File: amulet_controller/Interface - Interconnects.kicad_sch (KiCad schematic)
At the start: 57 parts, among them J10 JST S2B-PH-SM4-TB, J11 Nano-Fit 1x03, J12 Nano-Fit 1x03, J13 SM05B-GHS-TB, J14 PTH 01x02 2.54mm, J6 SM08B-GHS-TB, J7 SM07B-GHS-TB, J8 JST S2B-PH-SM4-TB, J9 SM06B-GHS-TB, SW1 CAS-220TA

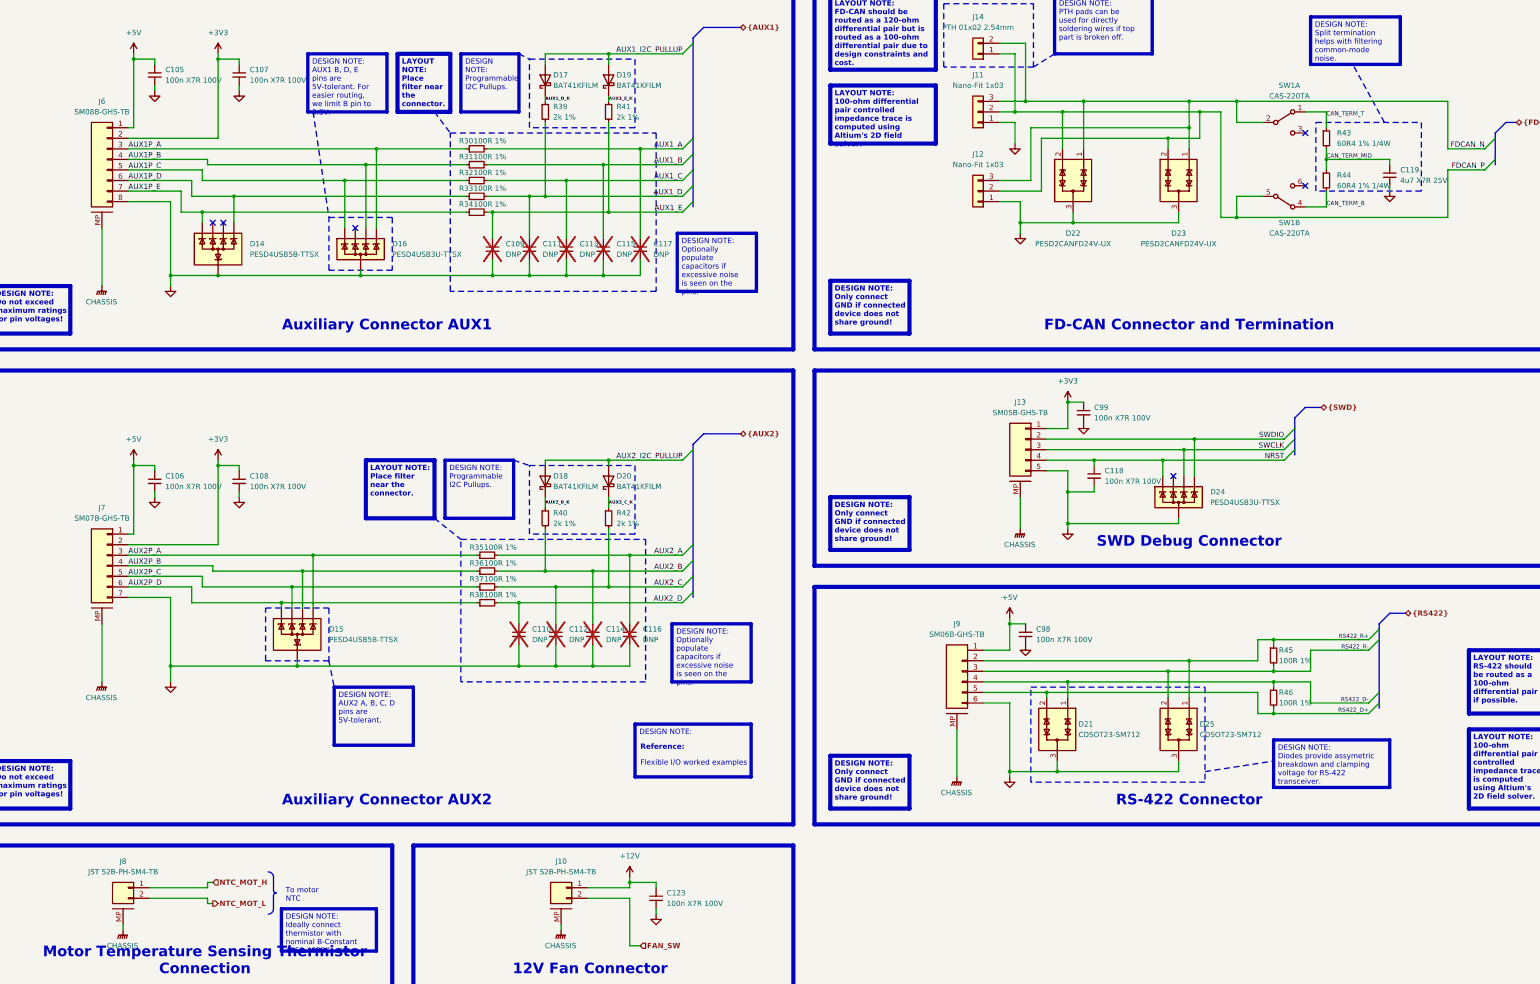
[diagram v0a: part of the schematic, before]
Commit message: filled in fields for bom, replaced inexisting components. Need to replace LEDs
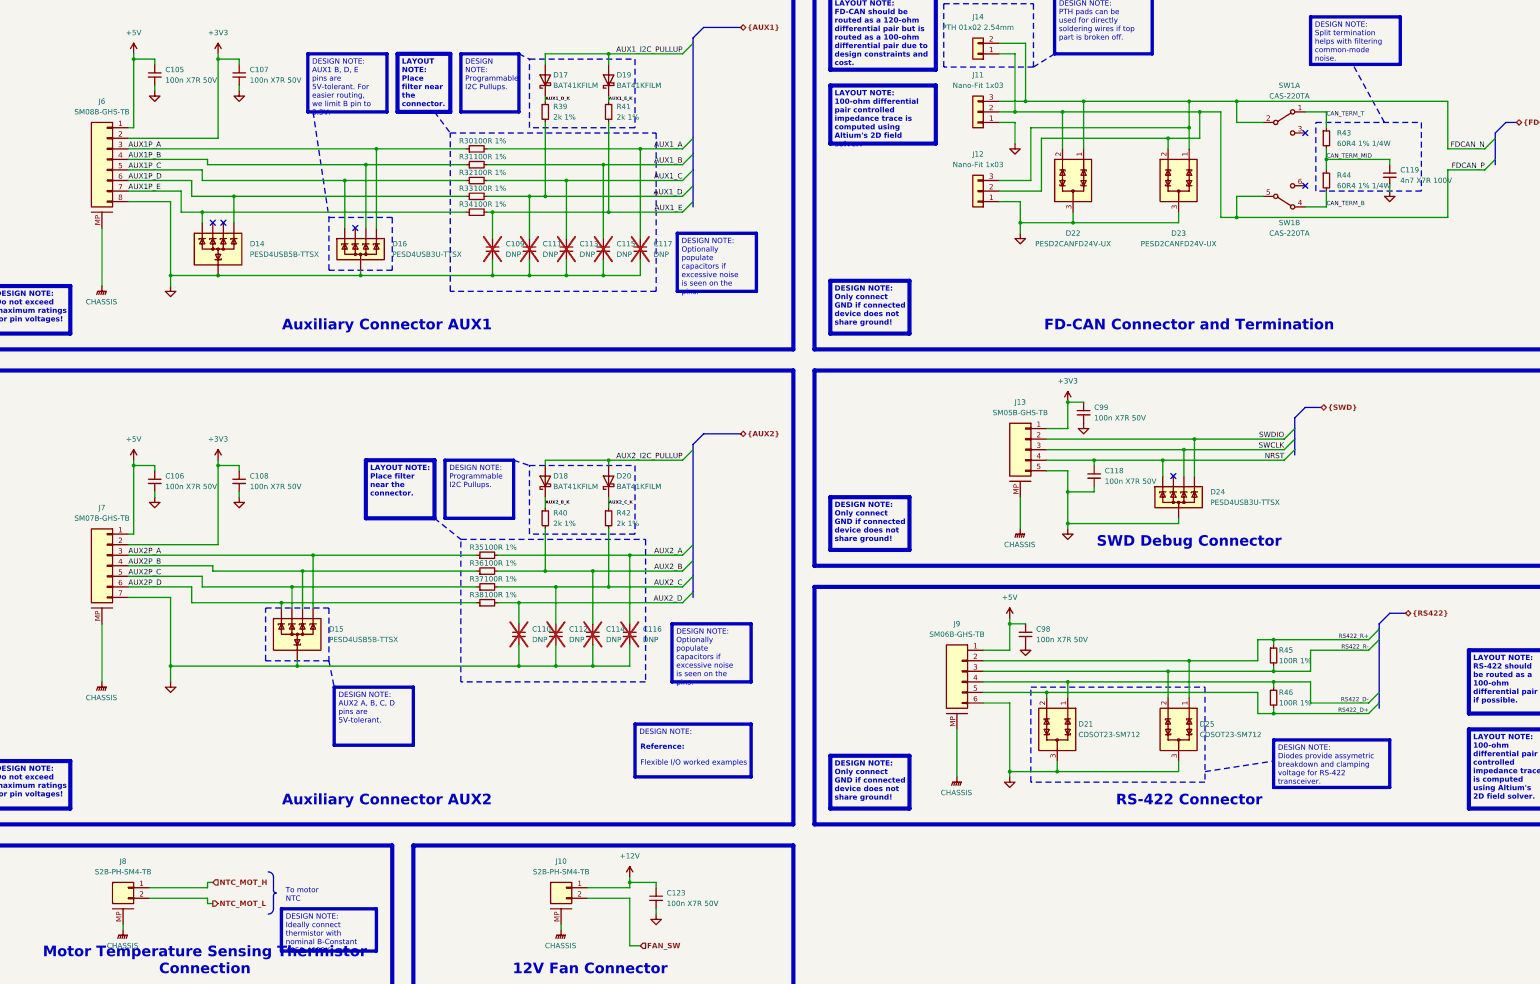
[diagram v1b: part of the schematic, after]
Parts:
- C105, C106, C107, C108, C118, C123, C98, C99: value 100n X7R 100V -> 100n X7R 50V; Manufacturer (none) -> Murata Electronics; Manufacturer Part Number (none) -> GCM155R71H104KE02J; Supplier 1 (none) -> Digikey; Supplier Part Number 1 (none) -> 490-14514-1-ND
- C119: value 4u7 X7R 25V -> 4n7 X7R 100V; Manufacturer (none) -> Murata Electronics; Manufacturer Part Number (none) -> GCM155R72A472KA37D; Supplier 1 (none) -> Digikey
- D14, D15: Manufacturer (none) -> Nexperia USA Inc.; Manufacturer Part Number (none) -> PESD4USB5B-TTSX; Supplier 1 (none) -> Digikey; Supplier Part Number 1 (none) -> 1727-PESD4USB5B-TTSXCT-ND
- D16, D24: Manufacturer (none) -> Nexperia USA Inc.; Manufacturer Part Number (none) -> PESD4USB3U-TTSX; Supplier 1 (none) -> Digikey; Supplier Part Number 1 (none) -> 1727-PESD4USB3U-TTSXCT-ND
- D17, D18, D19, D20: Manufacturer (none) -> STMicroelectronics; Manufacturer Part Number (none) -> BAT41KFILM; Supplier 1 (none) -> Digikey; Supplier Part Number 1 (none) -> 497-5556-1-ND
- D21, D25: Manufacturer (none) -> Bourns Inc.; Manufacturer Part Number (none) -> CDSOT23-SM712; Supplier 1 (none) -> Digikey; Supplier Part Number 1 (none) -> CDSOT23-SM712CT-ND
- D22, D23: Manufacturer (none) -> Nexperia USA Inc.; Manufacturer Part Number (none) -> PESD2CANFD24V-UX; Supplier 1 (none) -> Digikey; Supplier Part Number 1 (none) -> 1727-PESD2CANFD24V-UXCT-ND
- J10, J8: value JST S2B-PH-SM4-TB -> S2B-PH-SM4-TB; Manufacturer (none) -> JST Sales America Inc.; Manufacturer Part Number (none) -> S2B-PH-SM4-TB; Supplier 1 (none) -> Digikey; Supplier Part Number 1 (none) -> 455-S2B-PH-SM4-TBCT-ND
- J11, J12: Manufacturer (none) -> Molex; Manufacturer Part Number (none) -> 1054301203; Supplier 1 (none) -> Digikey; Supplier Part Number 1 (none) -> WM26098CT-ND
- J13: Manufacturer (none) -> JST Sales America Inc.; Manufacturer Part Number (none) -> SM05B-GHS-TB; Supplier 1 (none) -> Digikey; Supplier Part Number 1 (none) -> 455-SM05B-GHS-TBCT-ND
- J6: Manufacturer (none) -> JST Sales America Inc.; Manufacturer Part Number (none) -> SM08B-GHS-TB; Supplier 1 (none) -> Digikey; Supplier Part Number 1 (none) -> 455-1570-1-ND
- J7: Manufacturer (none) -> JST Sales America Inc.; Manufacturer Part Number (none) -> SM07B-GHS-TB; Supplier 1 (none) -> Digikey; Supplier Part Number 1 (none) -> 455-1569-1-ND
- J9: Manufacturer (none) -> JST Sales America Inc.; Manufacturer Part Number (none) -> SM06B-GHS-TB; Supplier 1 (none) -> Digikey; Supplier Part Number 1 (none) -> 455-1568-1-ND
- R30, R31, R32, R33, R34, R35, R36, R37, R38, R45, R46: Manufacturer (none) -> Panasonic Electronic Components; Manufacturer Part Number (none) -> ERJ-2RKF1000X; Supplier 1 (none) -> Digikey; Supplier Part Number 1 (none) -> P100LCT-ND
- R39, R40, R41, R42: Manufacturer (none) -> Vishay; Manufacturer Part Number (none) -> ERJ-2RKF2001X; Supplier 1 (none) -> Digikey; Supplier Part Number 1 (none) -> P2.00KLCT-ND
- R43, R44: Manufacturer (none) -> Rohm Semiconductor; Manufacturer Part Number (none) -> ESR03EZPF60R4; Supplier 1 (none) -> Digikey; Supplier Part Number 1 (none) -> 511-ESR03EZPF60R4CT-ND
- SW1: Manufacturer (none) -> Nidec Components Corporation

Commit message: added test points
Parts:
- removed D14, D15: PESD4USB5B-TTSX, 0_package_DFN_QFN:DFN2510-D10, symbol 0_power_protection:PESD4USB5B-TTSX
- removed D16, D24: PESD4USB3U-TTSX, 0_package_DFN_QFN:DFN2510-D10, symbol 0_power_protection:PESD4USB5B-TTSX_1
- removed J14: PTH 01x02 2.54mm, 0_connectors:PTH_1x02_P2.54mm, symbol Connector_Generic:Conn_01x02
- added D14, D15: PESD4USB5B-TBSX, 0_package_DFN_QFN:SOT1176D, symbol 0_power_protection:PESD4USB5B-TBSX
- added D16, D24: PESD4USB3U-TBSX, 0_package_DFN_QFN:SOT1176D, symbol 0_power_protection:PESD4USB3U-TBSX
- added J14: PTH 01x03 2.54mm, 0_connectors:PTH_1x03_P2.54mm, symbol Connector_Generic:Conn_01x03
- D21, D25: footprint 0_package_SOT_TO_SMD:SOT95P230X117-3N -> 0_package_SOT_TO_SMD:SOT95P230X110-3N
- R30, R31, R32, R33, R34, R35, R36, R37, R38, R45, R46: value 100R 1% -> 100R 1% 1/5W; Manufacturer Panasonic Electronic Components -> Vishay; Manufacturer Part Number ERJ-2RKF1000X -> RCS0402100RFKED; Supplier Part Number 1 P100LCT-ND -> 541-2886-1-ND
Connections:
- net AUX1P_A: now also D16.5 (K), D16.6 (K)
- net AUX1P_B: now also D16.4 (K), D16.7 (K)
- net AUX1P_C: now also D16.1 (K), D16.10 (K)
- net AUX1P_D: now also D14.5 (K), D14.6 (K)
- net AUX1P_E: now also D14.1 (K), D14.10 (K)
- net AUX2P_A: now also D15.5 (K), D15.6 (K)
- net AUX2P_B: now also D15.4 (K), D15.7 (K)
- net AUX2P_C: now also D15.2 (K), D15.9 (K)
- net AUX2P_D: now also D15.1 (K), D15.10 (K)
- net FDCAN_N: now also J14.3 (Pin_3)
- net FDCAN_P: now also J14.2 (Pin_2)
- net GND: now also D14.3 (A), D14.8 (A), D15.3 (A), D15.8 (A), D16.3 (A), D16.8 (A), D24.3 (A), D24.8 (A), J14.1 (Pin_1)
- net NRST: now also D24.1 (K), D24.10 (K)
- net SWCLK: now also D24.4 (K), D24.7 (K)
- net SWDIO: now also D24.5 (K), D24.6 (K)
- new net: D16.2 (K), D16.9 (K)
- new net: D14.2 (K), D14.9 (K)
- new net: D14.4 (K), D14.7 (K)
- new net: D24.2 (K), D24.9 (K)
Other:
- moved on the sheet: R45, R46

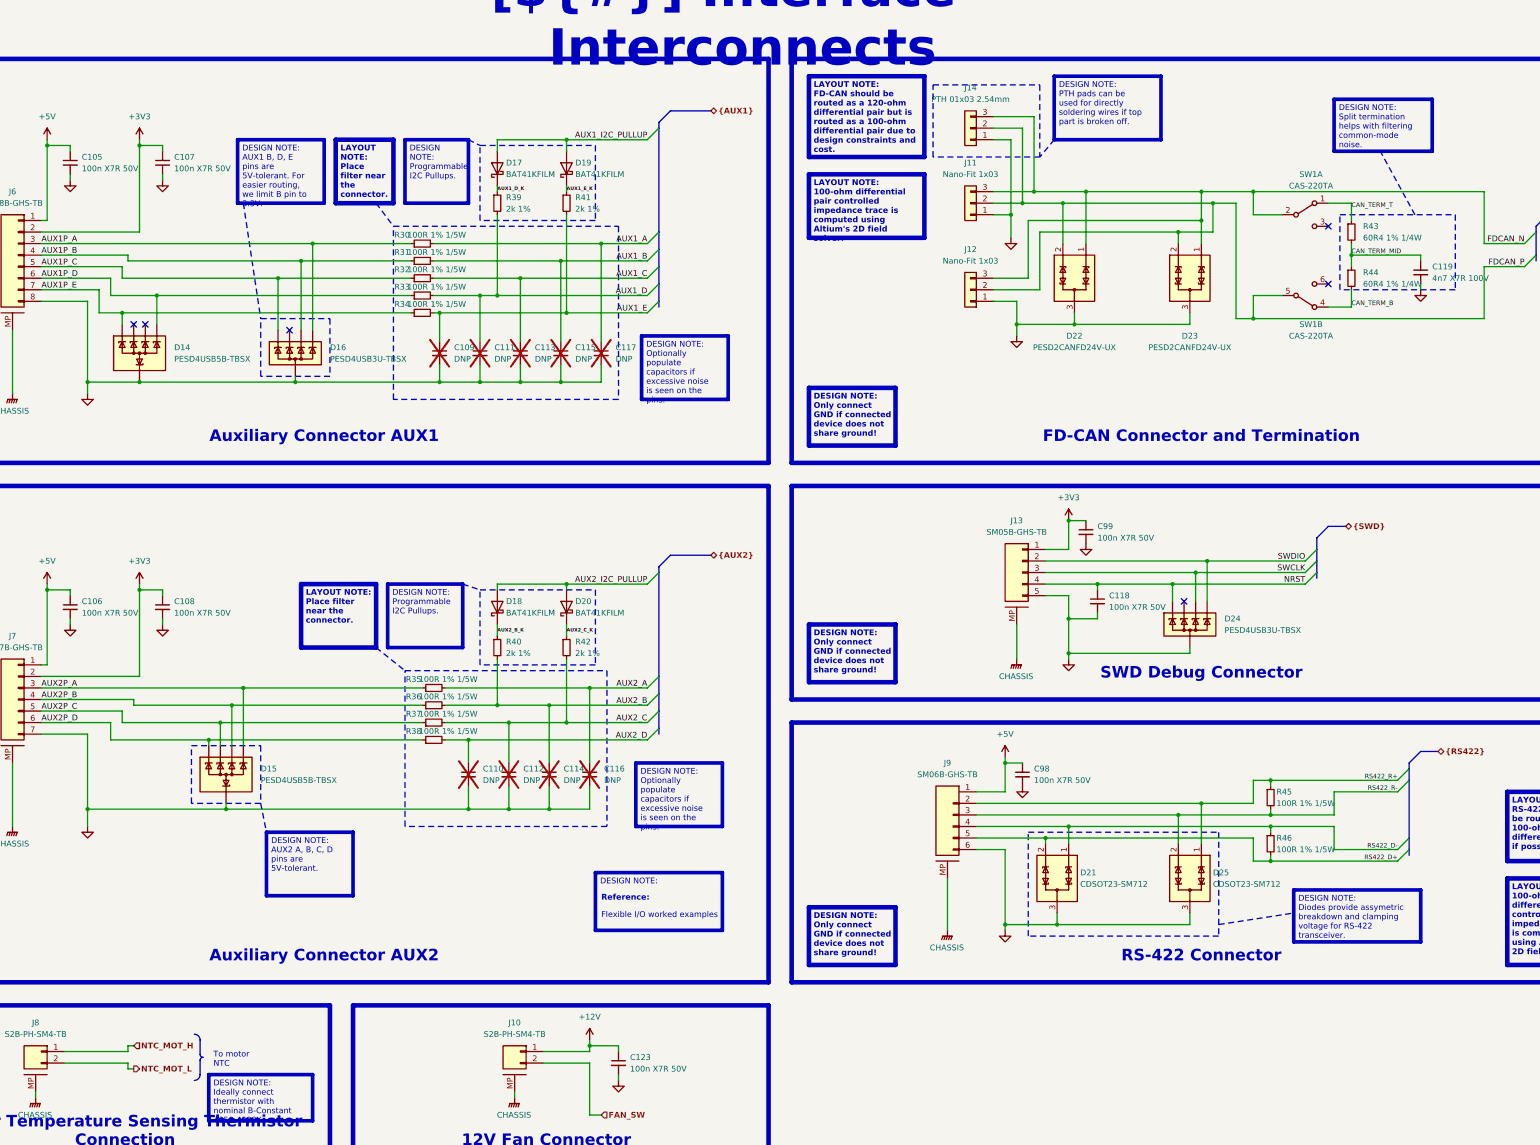
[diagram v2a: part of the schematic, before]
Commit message: finalized pcb. TODO: add clean BOM and KiBot integration
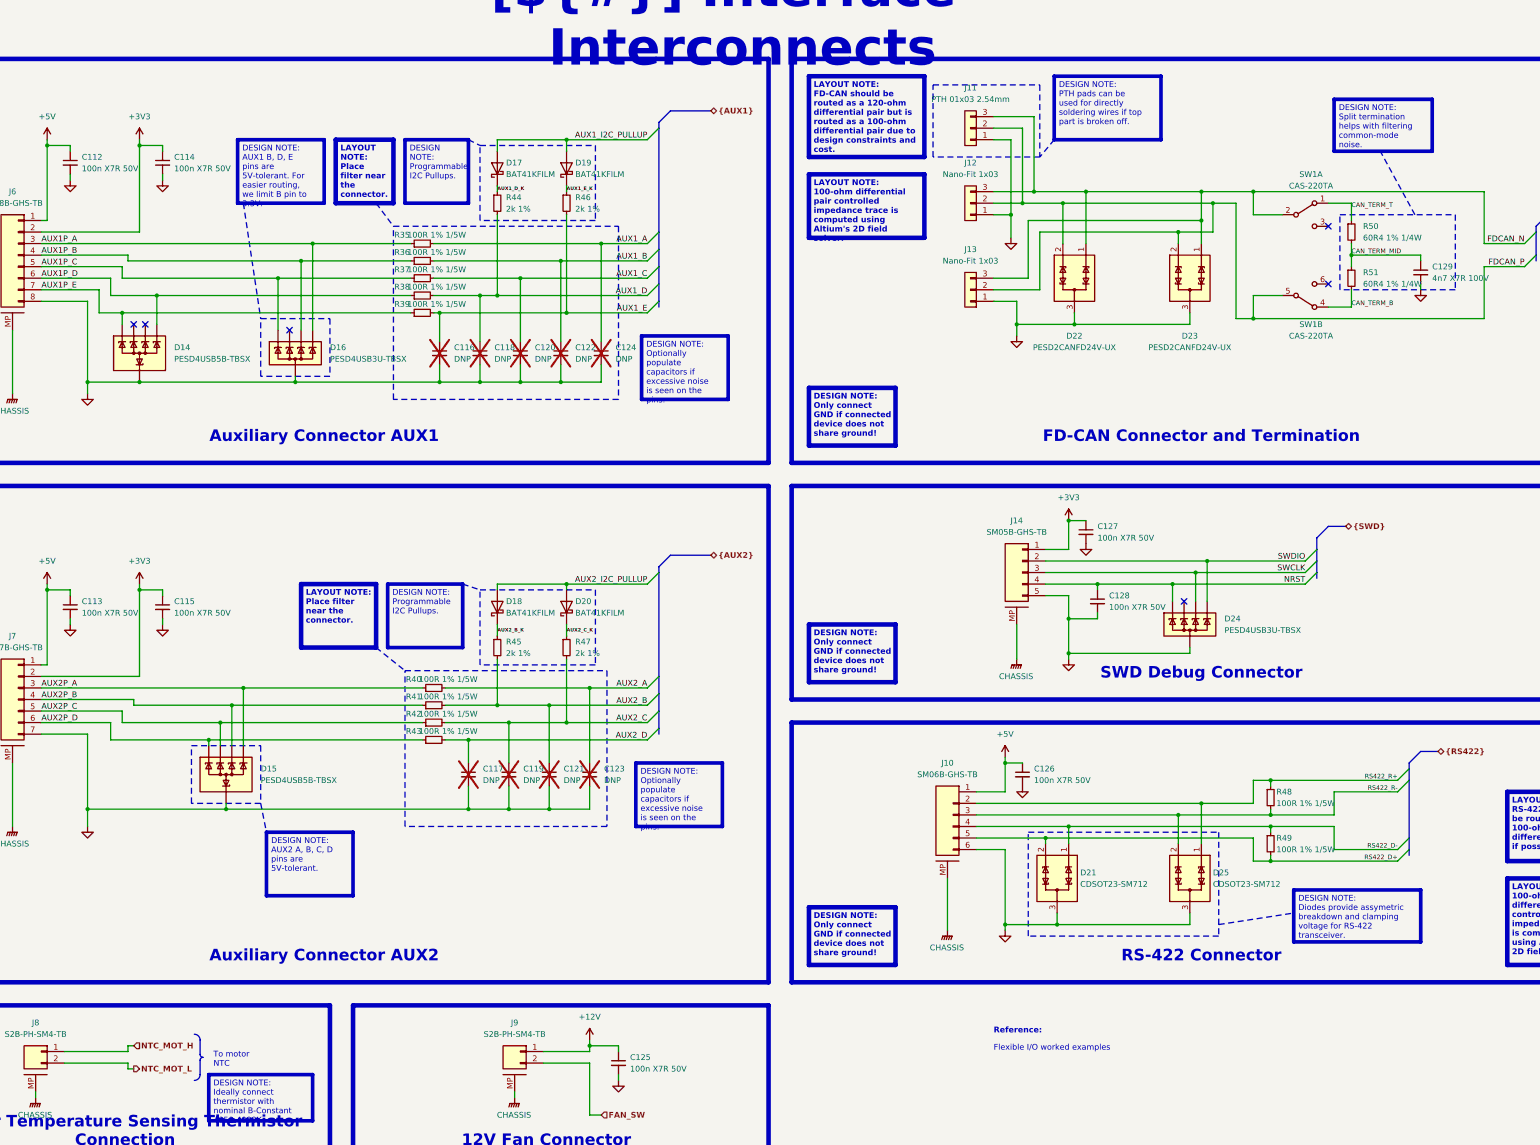
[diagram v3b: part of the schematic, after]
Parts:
- renumbered C105 to C112, C106 to C113, C107 to C114, C108 to C115, C109 to C116, C110 to C117, C111 to C118, C112 to C119, C113 to C120, C114 to C121, C115 to C122, C116 to C123, C117 to C124, C123 to C125, C98 to C126, C99 to C127, C118 to C128, C119 to C129, J9 to J10, J14 to J11, J11 to J12, J12 to J13, J13 to J14, J10 to J9, R30 to R35, R31 to R36, R32 to R37, R33 to R38, R34 to R39, R35 to R40, R36 to R41, R37 to R42, R38 to R43, R39 to R44, R40 to R45, R41 to R46, R42 to R47, R45 to R48, R46 to R49, R43 to R50, R44 to R51
